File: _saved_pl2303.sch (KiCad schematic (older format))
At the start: 23 parts, among them P2 USB_OTG, U2 PL2303, Y1 CRYSTAL

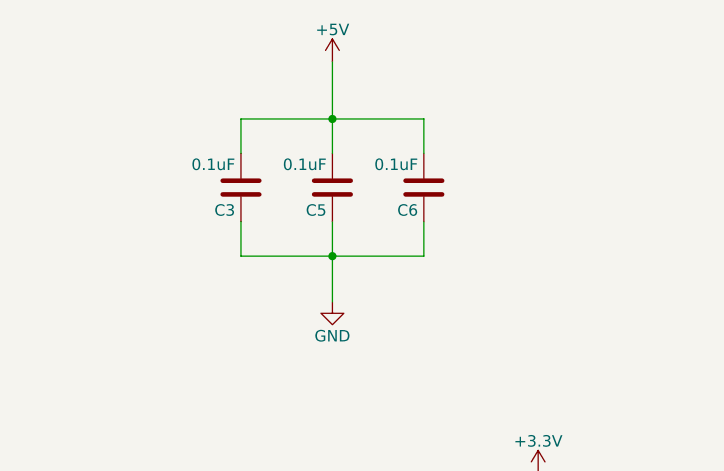
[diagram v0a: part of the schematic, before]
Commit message: Изменения футпринтов и расположения на плате
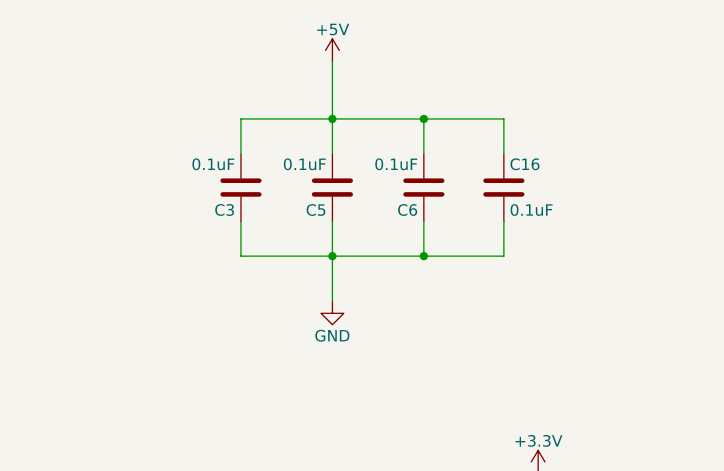
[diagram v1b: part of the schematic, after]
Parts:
- added C16: 0.1uF, Capacitors_SMD:C_0805, symbol C
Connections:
- net +5V: now also C16.1
- net GND: now also C16.2
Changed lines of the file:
@@
 	7900 1800 7900 1950
 Wire Wire Line
-	7900 1950 8700 1950
+	7900 1950 9050 1950
 Wire Wire Line
 	8700 1950 8700 1800
@@
 	7900 1350 7900 1500
 Wire Wire Line
-	7900 1350 8700 1350
+	7900 1350 9050 1350
 Wire Wire Line
 	8300 1100 8300 1500
@@
 	8500 5400 8650 5400
 NoConn ~ 8650 5300
+$Comp
+L C C16
+U 1 1 5739D45A
+P 9050 1650
+F 0 "C16" H 9075 1750 50  0000 L CNN
+F 1 "0.1uF" H 9075 1550 50  0000 L CNN
+F 2 "Capacitors_SMD:C_0805" H 9088 1500 50  0001 C CNN
+F 3 "" H 9050 1650 50  0000 C CNN
+	1    9050 1650
+	1    0    0    -1
+$EndComp
+Wire Wire Line
+	9050 1350 9050 1500
+Connection ~ 8700 1350
+Wire Wire Line
+	9050 1950 9050 1800
+Connection ~ 8700 1950
 $EndSCHEMATC
